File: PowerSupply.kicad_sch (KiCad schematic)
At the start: 5 parts, among them U1 AMS1117-3.3

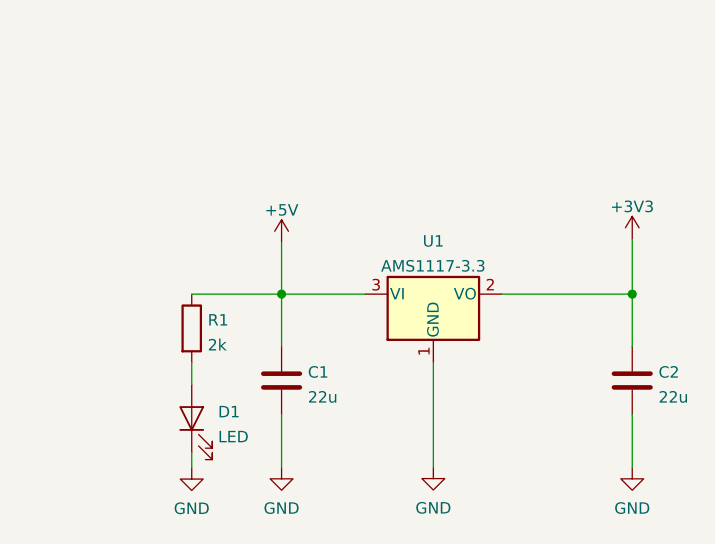
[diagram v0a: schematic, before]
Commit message: Routed most PCB traces
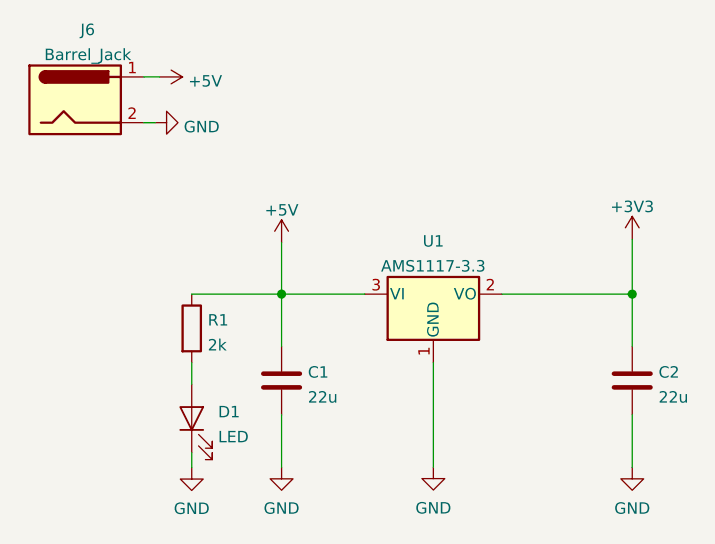
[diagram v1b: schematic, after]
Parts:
- added J6: Barrel_Jack, Connector_BarrelJack:BarrelJack_CLIFF_FC681465S_SMT_Horizontal, symbol Connector:Barrel_Jack
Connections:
- net +5V: now also J6.1
- net GND: now also J6.2
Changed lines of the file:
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@@
   (junction (at 125.5522 86.868) (diameter 1.016) (color 0 0 0 0))
   (junction (at 164.5158 86.868) (diameter 1.016) (color 0 0 0 0))
+  (wire (pts (xy 110.236 62.738) (xy 112.014 62.738))
+    (stroke (width 0) (type solid) (color 0 0 0 0))
+  )
+  (wire (pts (xy 110.236 67.818) (xy 111.506 67.818))
+    (stroke (width 0) (type solid) (color 0 0 0 0))
+  )
   (wire (pts (xy 115.57 86.868) (xy 125.5522 86.868))
     (stroke (width 0) (type solid) (color 0 0 0 0))
@@
   (wire (pts (xy 164.5158 100.2792) (xy 164.5158 106.1212))
     (stroke (width 0) (type solid) (color 0 0 0 0))
+  )
+  (symbol (lib_id "power:+5V") (at 112.014 62.738 270) (unit 1)
+    (in_bom yes) (on_board yes) (fields_autoplaced)
+    (property "Reference" "#EXT_5v01" (id 0) (at 108.204 62.738 0)
+      (effects (font (size 1.27 1.27)) hide)
+    )
+    (property "Value" "+5V" (id 1) (at 115.1891 63.217 90)
+      (effects (font (size 1.27 1.27)) (justify left))
+    )
+    (property "Footprint" "" (id 2) (at 112.014 62.738 0)
+      (effects (font (size 1.27 1.27)) hide)
+    )
+    (property "Datasheet" "" (id 3) (at 112.014 62.738 0)
+      (effects (font (size 1.27 1.27)) hide)
+    )
+    (pin "1")
   )
   (symbol (lib_id "power:+5V") (at 125.5522 81.153 0) (unit 1)
@@
     (pin "1")
   )
+  (symbol (lib_id "power:GND") (at 111.506 67.818 90) (unit 1)
+    (in_bom yes) (on_board yes) (fields_autoplaced)
+    (property "Reference" "#PWR01" (id 0) (at 117.856 67.818 0)
+      (effects (font (size 1.27 1.27)) hide)
+    )
+    (property "Value" "GND" (id 1) (at 114.6811 68.297 90)
+      (effects (font (size 1.27 1.27)) (justify right))
+    )
+    (property "Footprint" "" (id 2) (at 111.506 67.818 0)
+      (effects (font (size 1.27 1.27)) hide)
+    )
+    (property "Datasheet" "" (id 3) (at 111.506 67.818 0)
+      (effects (font (size 1.27 1.27)) hide)
+    )
+    (pin "1")
+  )
   (symbol (lib_id "power:GND") (at 115.57 106.1466 0) (unit 1)
     (in_bom yes) (on_board yes) (fields_autoplaced)
@@
       (effects (font (size 1.27 1.27)) hide)
     )
+    (pin "1")
+    (pin "2")
+  )
+  (symbol (lib_id "Connector:Barrel_Jack") (at 102.616 65.278 0) (unit 1)
+    (in_bom yes) (on_board yes) (fields_autoplaced)
+    (property "Reference" "J6" (id 0) (at 104.013 57.5014 0))
+    (property "Value" "Barrel_Jack" (id 1) (at 104.013 60.2765 0))
+    (property "Footprint" "Connector_BarrelJack:BarrelJack_CLIFF_FC681465S_SMT_Horizontal" (id 2) (at 103.886 66.294 0)
+      (effects (font (size 1.27 1.27)) hide)
+    )
+    (property "Datasheet" "~" (id 3) (at 103.886 66.294 0)
+      (effects (font (size 1.27 1.27)) hide)
+    )

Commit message: Added VOC and Optical Sensors
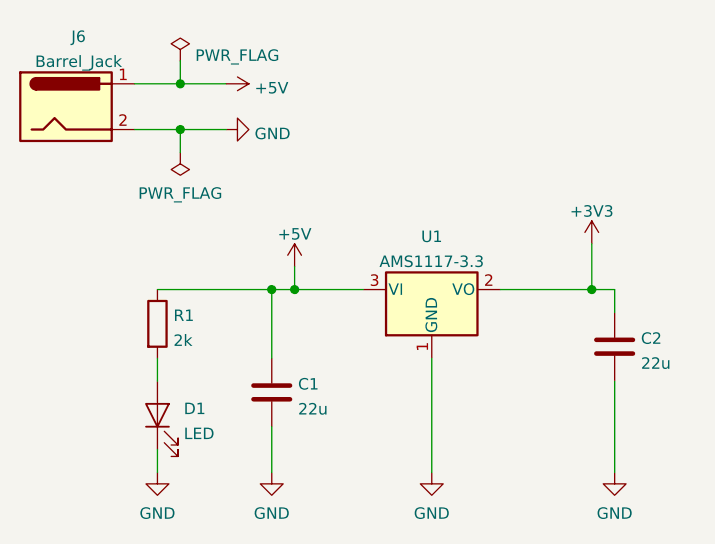
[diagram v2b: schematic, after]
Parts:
- J6: footprint Connector_BarrelJack:BarrelJack_CLIFF_FC681465S_SMT_Horizontal -> Connector_BarrelJack:BarrelJack_CUI_PJ-063AH_Horizontal
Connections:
- net +5V: now also C1.1, R1.1, U1.3 (VI)
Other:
- moved on the sheet: C1, C2, D1, J6, R1, U1

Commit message: Vertical Horizontal Traces
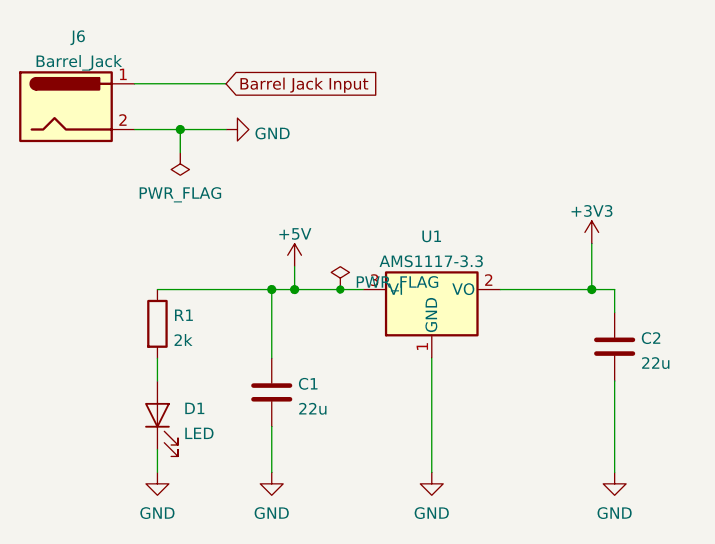
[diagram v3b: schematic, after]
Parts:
- R1: footprint Resistor_SMD:R_0603_1608Metric -> Resistor_SMD:R_0603_1608Metric_Pad0.98x0.95mm_HandSolder
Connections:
- net +5V: no longer J6.1
- new net Barrel Jack Input: J6.1
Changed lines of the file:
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@@
 (kicad_sch (version 20210621) (generator eeschema)
   (paper "A4")
-  (junction (at 114.3 63.5) (diameter 1.016) (color 0 0 0 0))
   (junction (at 114.3 68.58) (diameter 1.016) (color 0 0 0 0))
   (junction (at 124.46 86.36) (diameter 1.016) (color 0 0 0 0))
   (junction (at 127 86.36) (diameter 1.016) (color 0 0 0 0))
+  (junction (at 132.08 86.36) (diameter 0) (color 0 0 0 0))
   (junction (at 160.02 86.36) (diameter 1.016) (color 0 0 0 0))
-  (wire (pts (xy 109.22 63.5) (xy 114.3 63.5))
+  (wire (pts (xy 109.22 63.5) (xy 119.38 63.5))
     (stroke (width 0) (type solid) (color 0 0 0 0))
   )
@@
     (stroke (width 0) (type solid) (color 0 0 0 0))
   )
-  (wire (pts (xy 114.3 60.96) (xy 114.3 63.5))
-    (stroke (width 0) (type solid) (color 0 0 0 0))
-  )
-  (wire (pts (xy 114.3 63.5) (xy 119.38 63.5))
-    (stroke (width 0) (type solid) (color 0 0 0 0))
-  )
   (wire (pts (xy 114.3 68.58) (xy 114.3 71.12))
     (stroke (width 0) (type solid) (color 0 0 0 0))
@@
     (stroke (width 0) (type solid) (color 0 0 0 0))
   )
-  (wire (pts (xy 127 86.36) (xy 134.62 86.36))
+  (wire (pts (xy 127 86.36) (xy 132.08 86.36))
+    (stroke (width 0) (type solid) (color 0 0 0 0))
+  )
+  (wire (pts (xy 132.08 86.36) (xy 134.62 86.36))
     (stroke (width 0) (type solid) (color 0 0 0 0))
   )
@@
     (stroke (width 0) (type solid) (color 0 0 0 0))
   )
-  (symbol (lib_id "power:+5V") (at 119.38 63.5 270) (unit 1)
-    (in_bom yes) (on_board yes) (fields_autoplaced)
-    (property "Reference" "#EXT_5v01" (id 0) (at 115.57 63.5 0)
-      (effects (font (size 1.27 1.27)) hide)
-    )
-    (property "Value" "+5V" (id 1) (at 122.5551 63.979 90)
-      (effects (font (size 1.27 1.27)) (justify left))
-    )
-    (property "Footprint" "" (id 2) (at 119.38 63.5 0)
-      (effects (font (size 1.27 1.27)) hide)
-    )
-    (property "Datasheet" "" (id 3) (at 119.38 63.5 0)
-      (effects (font (size 1.27 1.27)) hide)
-    )
-    (pin "1")
+  (global_label "Barrel Jack Input" (shape input) (at 119.38 63.5 0) (fields_autoplaced)
+    (effects (font (size 1.27 1.27)) (justify left))
+    (property "Intersheet References" "${INTERSHEET_REFS}" (id 0) (at 138.4845 63.5794 0)
+      (effects (font (size 1.27 1.27)) (justify left) hide)
+    )
   )
   (symbol (lib_id "power:+5V") (at 127 83.82 0) (unit 1)
@@
     (pin "1")
   )
-  (symbol (lib_id "power:PWR_FLAG") (at 114.3 60.96 0) (unit 1)
-    (in_bom yes) (on_board yes) (fields_autoplaced)
-    (property "Reference" "#FLG0102" (id 0) (at 114.3 59.055 0)
-      (effects (font (size 1.27 1.27)) hide)
-    )
-    (property "Value" "PWR_FLAG" (id 1) (at 115.9511 60.3595 0)
-      (effects (font (size 1.27 1.27)) (justify left))
-    )
-    (property "Footprint" "" (id 2) (at 114.3 60.96 0)
-      (effects (font (size 1.27 1.27)) hide)
-    )
-    (property "Datasheet" "~" (id 3) (at 114.3 60.96 0)
-      (effects (font (size 1.27 1.27)) hide)
-    )
-    (pin "1")
-  )
   (symbol (lib_id "power:PWR_FLAG") (at 114.3 71.12 180) (unit 1)
     (in_bom yes) (on_board yes) (fields_autoplaced)
@@
     (pin "1")
   )
+  (symbol (lib_id "power:PWR_FLAG") (at 132.08 86.36 0) (unit 1)
+    (in_bom yes) (on_board yes) (fields_autoplaced)
+    (property "Reference" "#FLG0106" (id 0) (at 132.08 84.455 0)
+      (effects (font (size 1.27 1.27)) hide)
+    )
+    (property "Value" "PWR_FLAG" (id 1) (at 133.731 85.569 0)
+      (effects (font (size 1.27 1.27)) (justify left))
+    )
+    (property "Footprint" "" (id 2) (at 132.08 86.36 0)
+      (effects (font (size 1.27 1.27)) hide)
+    )
+    (property "Datasheet" "~" (id 3) (at 132.08 86.36 0)
+      (effects (font (size 1.27 1.27)) hide)
+    )
+    (pin "1")
+  )
   (symbol (lib_id "power:GND") (at 111.76 106.68 0) (unit 1)
     (in_bom yes) (on_board yes) (fields_autoplaced)
@@
       (effects (font (size 1.27 1.27)) (justify left))
     )
-    (property "Footprint" "Resistor_SMD:R_0603_1608Metric" (id 2) (at 109.982 90.17 90)
-      (effects (font (size 1.27 1.27)) hide)
-    )
+    (property "Footprint" "Resistor_SMD:R_0603_1608Metric_Pad0.98x0.95mm_HandSolder" (id 2) (at 109.982 90.17 90)
+      (effects (font (size 1.27 1.27)) hide)
+    )
